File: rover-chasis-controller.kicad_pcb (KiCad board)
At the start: 2 copper layers, 86 x 97 mm, 82 parts, among them J1 Motor control, J11 Compass Connection (I2C), J15 External LED (Red), J16 External LED (Yellow), J17 External LED (Green), J2 Motor control, J22 Ultrasonic Sensor Inputs, J3 Motor control, J38 Motor control, J4 Screw_Terminal_01x02, J40 Encoder, J41 Encoder, J42 Encoder, J43 Encoder, J7 TTL, J8 Ultrasonic Sensor Inputs, Q14 MMBT3904_C181119, Q2 HSBA100P04_C2987717, Q33 MMBT3904_C181119, Q34 MMBT3904_C181119, Q35 MMBT3904_C181119, U1 APT2012LVBC/D, U2 APT2012LVBC/D, U3 APT2012LVBC/D, U4 AP64500, U5 MPU-6050_C24112, U6 PCA9685PW,118, U7 APT2012LVBC/D

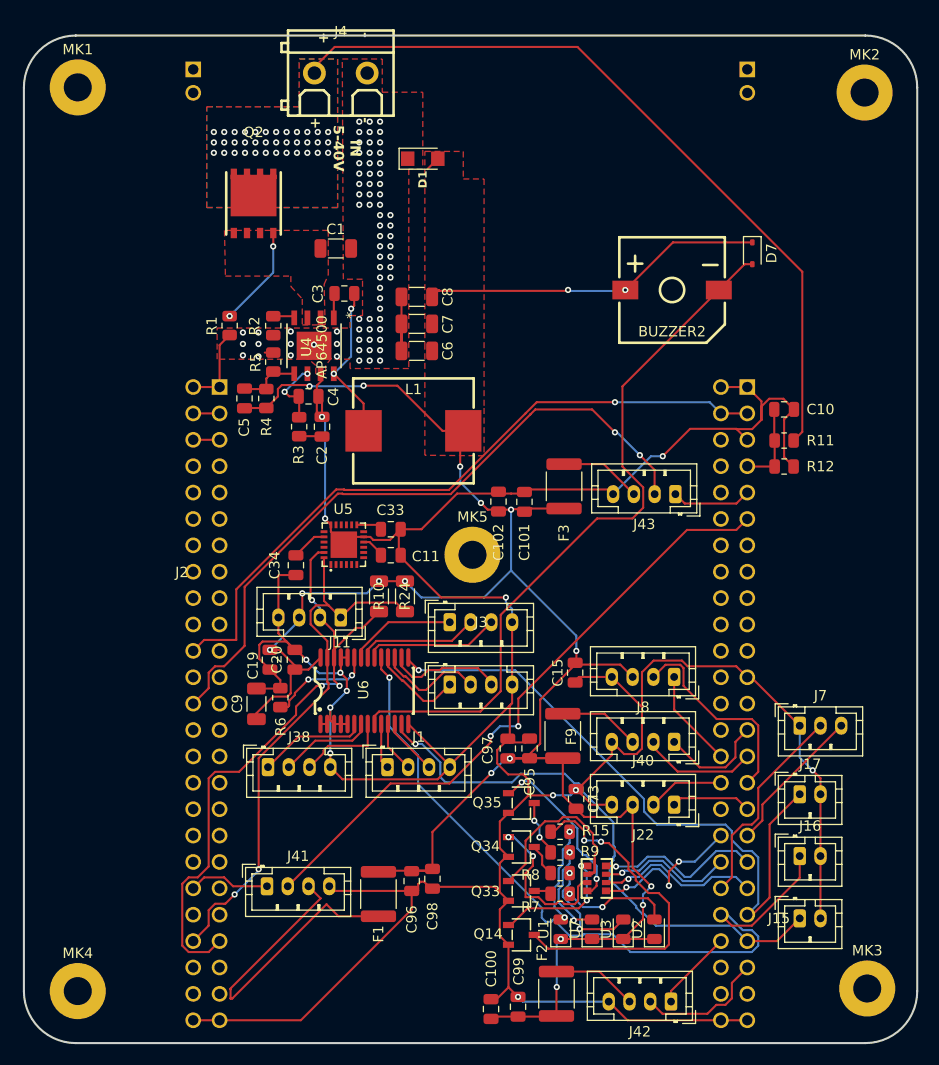
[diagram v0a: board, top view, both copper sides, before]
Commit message: Board malfunction fixes
- Changed F1-F4, R5, R6 to 3V (previous 5V caused failure).

- Connected STM32DISC1 to 5V and 3V outputs/inputs

- Moved SDA to PC9 (was PA9) and ENC3_A to PC6 (was PC3).

- Redesigned MPU6050 layout to resolve stability and connectivity issues.

- Isolated PCA6587 buzzer with a transistor.
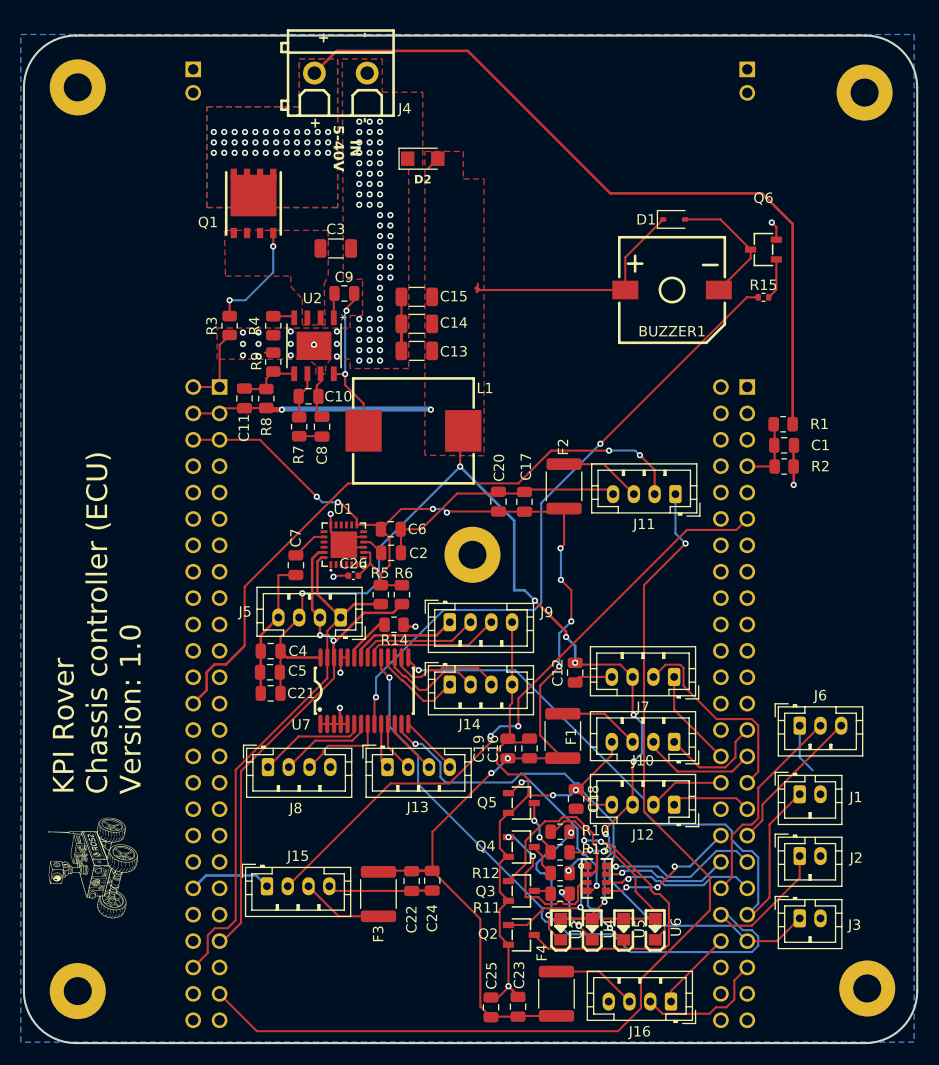
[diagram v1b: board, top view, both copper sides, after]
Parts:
- added C26: 10nF, Capacitor_SMD:C_0402_1005Metric, F.Cu at (63.0, 95.1)
- added G***: LOGO, kpi-rover:kpi-rover-logo, F.Cu at (37.8, 123.2)
- added Q6: MMBT3904_C181119, easyeda2kicad:SOT-23-3_L2.9-W1.6-P1.90-LS2.8-BR, F.Cu at (102.5, 63.7)
- added R15: 1k, Resistor_SMD:R_0402_1005Metric, F.Cu at (102.5, 68.3)
- C16: renamed from C95; value 10uF -> 10uFx16V
- C17: renamed from C101; value 10uF -> 10uFx16V
- C21: renamed from C9; value 10uF -> 10uFx16V; footprint Capacitor_SMD:C_1206_3216Metric -> Capacitor_SMD:C_0805_2012Metric
- C22: renamed from C96; value 10uF -> 10uFx16V
- C23: renamed from C99; value 10uF -> 10uFx16V
- C3: renamed from C1; value 10uF -> 10uFx50V
- C5: renamed from C19; value 10uF -> 10uFx16V
- R5: renamed from R24; footprint Resistor_SMD:R_1206_3216Metric -> Resistor_SMD:R_0805_2012Metric
- R6: renamed from R10; footprint Resistor_SMD:R_1206_3216Metric -> Resistor_SMD:R_0805_2012Metric
- U3: renamed from U1; footprint LED_SMD:LED_0805_2012Metric -> easyeda2kicad:LED-SMD_L2.0-W1.3-R-RD
- U4: renamed from U2; footprint LED_SMD:LED_0805_2012Metric -> easyeda2kicad:LED-SMD_L2.0-W1.3-R-RD
- U5: renamed from U3; footprint LED_SMD:LED_0805_2012Metric -> easyeda2kicad:LED-SMD_L2.0-W1.3-R-RD
- U6: renamed from U7; footprint LED_SMD:LED_0805_2012Metric -> easyeda2kicad:LED-SMD_L2.0-W1.3-R-RD
- moved R14 13.0 mm to (66.9, 99.8), turned to 180 degrees
- moved D1 8.20 mm to (93.9, 60.8), turned to 0 degrees
- moved U6 6.07 mm to (92.1, 129.1)
- moved U4 5.99 mm to (86.0, 129.1)
- moved C1 3.46 mm to (104.5, 82.5)
- moved C4 2.47 mm to (55.1, 102.4), turned to 0 degrees
- moved R5 2.33 mm to (65.7, 96.9)
- moved R6 2.21 mm to (67.7, 96.9)
- moved C21 1.70 mm to (55.1, 106.4), turned to 180 degrees
- moved R1 1.57 mm to (104.4, 80.5)
- moved C5 1.21 mm to (55.0, 104.4), turned to 0 degrees
- moved C2 0.23 mm to (66.7, 92.9)
- moved C24 0.18 mm to (70.6, 124.5)
- moved C25 0.16 mm to (76.3, 136.7)
- renumbered BUZZER2 to BUZZER1, C10 to C1, C4 to C10, C5 to C11, C15 to C12, C6 to C13, C7 to C14, C8 to C15, C73 to C18, C97 to C19, C11 to C2, C102 to C20, C98 to C24, C100 to C25, C20 to C4, C33 to C6, C34 to C7, C2 to C8, C3 to C9, D7 to D1, D1 to D2, F9 to F1, F3 to F2, F1 to F3, F2 to F4, J17 to J1, J40 to J10, J43 to J11, J22 to J12, J1 to J13, J3 to J14, J41 to J15, J42 to J16, J16 to J2, J15 to J3, J11 to J5, J7 to J6, J8 to J7, J38 to J8, J2 to J9, MK5 to MK1, MK1 to MK2, MK2 to MK3, MK3 to MK4, MK4 to MK5, Q2 to Q1, Q14 to Q2, Q33 to Q3, Q34 to Q4, Q35 to Q5, R11 to R1, R15 to R10, R7 to R11, R8 to R12, R9 to R13, R6 to R14, R12 to R2, R1 to R3, R2 to R4, R3 to R7, R4 to R8, R5 to R9, U5 to U1, U4 to U2, U6 to U7
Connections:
- BUZZER1 pad 2: /BUZZER_OUT -> Net-(BUZZER1--)
- C16 pad 2: VCC (5V) -> VDD (3V)
- C17 pad 2: VCC (5V) -> VDD (3V)
- C19 pad 2: VCC (5V) -> VDD (3V)
- C20 pad 2: VCC (5V) -> VDD (3V)
- C22 pad 2: VCC (5V) -> VDD (3V)
- C23 pad 2: VCC (5V) -> VDD (3V)
- C24 pad 2: VCC (5V) -> VDD (3V)
- C25 pad 2: VCC (5V) -> VDD (3V)
- D1 pad 2: /BUZZER_OUT -> Net-(BUZZER1--)
- F1 pad 2: VCC (5V) -> VDD (3V)
- F2 pad 2: VCC (5V) -> VDD (3V)
- F3 pad 2: VCC (5V) -> VDD (3V)
- F4 pad 2: VCC (5V) -> VDD (3V)
- R5 pad 1: VCC (5V) -> VDD (3V)
- R6 pad 1: VCC (5V) -> VDD (3V)
- TB1 pad P1_9: /ENC3_A -> unconnected-(TB1-PC3-PadP1_9)
- TB1 pad P2_3: Net-(TB1-5V-PadP2_3) -> VCC (5V)
- TB1 pad P2_4: Net-(TB1-5V-PadP2_3) -> VCC (5V)
- TB1 pad P2_44: /SDA -> unconnected-(TB1-PA9-PadP2_44)
- TB1 pad P2_46: unconnected-(TB1-PC9-PadP2_46) -> /SDA
- TB1 pad P2_47: unconnected-(TB1-PC6-PadP2_47) -> /ENC3_A
- TB1 pad P2_5: Net-(TB1-3V-PadP2_5) -> VDD (3V)
- TB1 pad P2_6: Net-(TB1-3V-PadP2_5) -> VDD (3V)
- U1 pad 8: unconnected-(U5-VLOGIC-Pad8) -> VDD (3V)
- U1 pad 9: unconnected-(U5-AD0-Pad9) -> GND
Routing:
- net GND: track 374.3 -> 171.1 mm, vias 85 -> 82
- net VDD (3V): track 2.67 -> 130.3 mm, vias 0 -> 10
- net /ENC3_A: track 7.73 -> 99.9 mm, vias 0 -> 1
- net VCC (5V): track 232.9 -> 159.3 mm, vias 18 -> 11
- net Net-(TB1-VDD-PadP1_3): track 66.6 -> 0.00 mm, vias 1 -> 0
- net Net-(J15-Pin_3): track 33.4 -> 7.93 mm
- net Net-(BUZZER1--): track 0.00 -> 12.7 mm
- net /SCL: track 60.3 -> 53.1 mm, vias 3 -> 2
- net /BUZZER_OUT: track 69.1 -> 62.1 mm, vias 0 -> 2
- net Net-(U6-K): track 9.39 -> 15.7 mm
- net Net-(U7-~{OE}): track 10.4 -> 4.68 mm, vias 2 -> 0
- net Net-(U4-K): track 10.7 -> 5.80 mm
- net Net-(U3-K): track 9.71 -> 14.1 mm
- net Net-(Q6-Pad1): track 0.00 -> 3.95 mm
- net /ENC3_B: track 65.1 -> 61.9 mm
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- added copper zone on B.Cu, net GND
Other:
- board text added: "KPI Rover Chassis controller (ECU) Version: 1.0"
